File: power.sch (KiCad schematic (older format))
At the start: 21 parts, among them Q1 Q_NMOS_DGS, U7 TPS63060, U8 TPS22929D

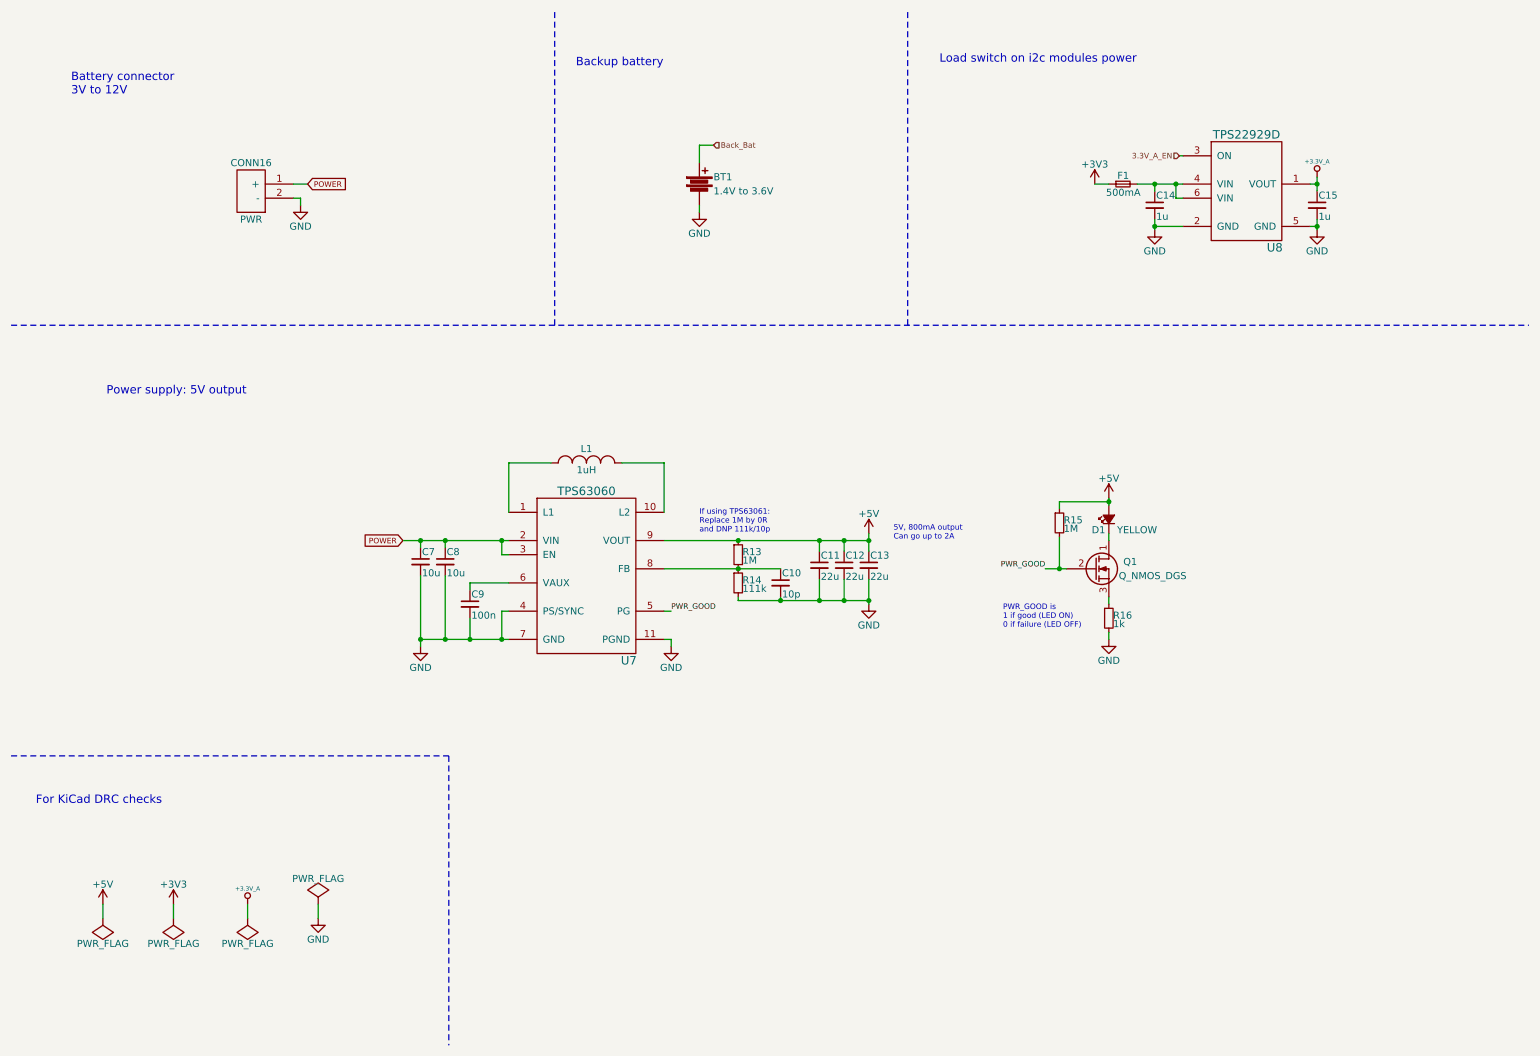
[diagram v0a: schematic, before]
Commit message: Schematics: Minor cleanups & ADC split between 3.3V & 5V
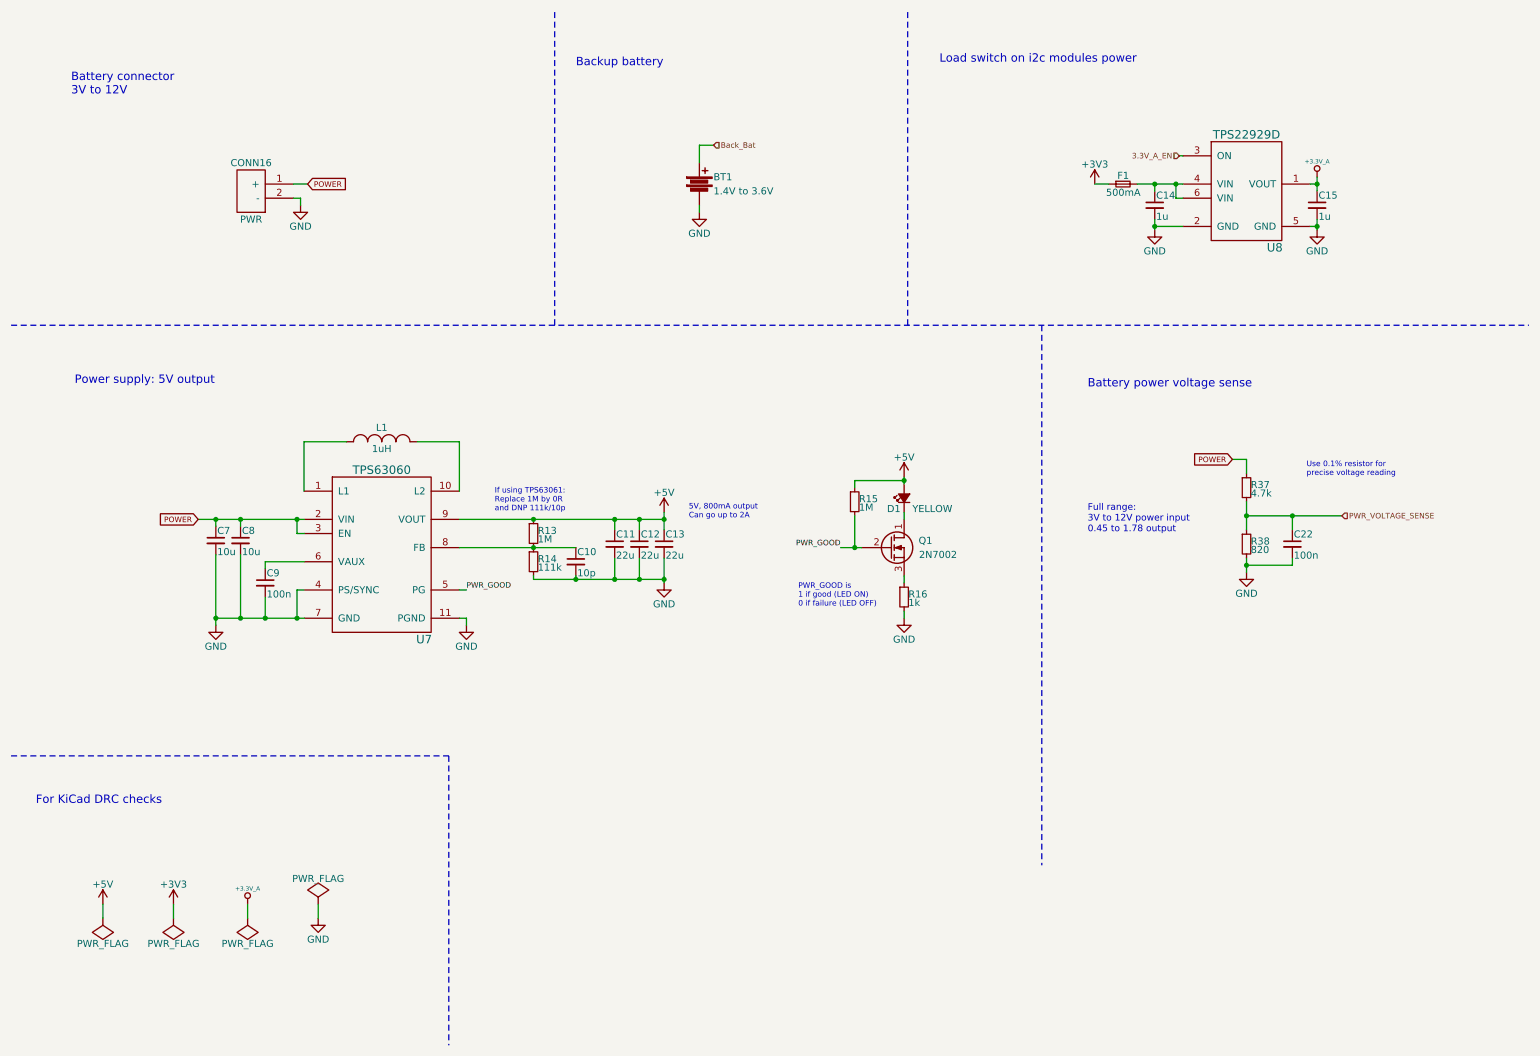
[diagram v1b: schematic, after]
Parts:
- added C22: 100n, symbol C_Small
- added R37: 4.7k, symbol R_Small
- added R38: 820, symbol R_Small
- C10, C11, C12, C13, C14, C15, C7, C8, C9, R13, R14, R15, R16: footprint (none) -> _std:_0402
- CONN16: footprint MODULE -> _connectors:_Pin2mm_2
- Q1: value Q_NMOS_DGS -> 2N7002
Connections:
- net GND: now also C22.2, R38.2
- net POWER: now also R37.1
- new net PWR_VOLTAGE_SENSE: C22.1, R37.2, R38.1
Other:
- note added: "Battery power voltage sense"
- note added: "Full range:\n3V to 12V power input\n0.45 to 1.78 output\n\n"
- note added: "Use 0.1% resistor for \nprecise voltage reading"
- moved on the sheet: C10, C11, C12, C13, C7, C8, C9, D1, L1, Q1, R13, R14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

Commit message: Schematics: Power input overvoltage protection
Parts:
- added D6: ZENER 12V, symbol ZENER
- added F2: 10A, symbol FUSE
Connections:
- net GND: now also D6.2 (A)
- net POWER: now also D6.1 (K), F2.2; no longer CONN16.1 (+)
- new net: CONN16.1 (+), F2.1
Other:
- note added: "Backup battery for RTC"
- note added: "Choose the fuse depending on the type of battery \nyou're using (check the maximum current it can \noutput) so the fuse blows before the battery."
- note added: "Zener diode acts as overvoltage \nprotection. \nWhen input voltage exceeds 12V,\nthe zener diode short circuits the \nbattery to the ground and the fuse \nshould blow."
- note removed: "Backup battery"
- moved on the sheet: CONN16
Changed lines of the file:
@@
 L PWR CONN16
 U 1 1 55AAEB82
-P 2125 1750
-F 0 "CONN16" H 2075 1950 50  0000 C CNN
-F 1 "PWR" H 2075 1550 50  0000 C CNN
-F 2 "_connectors:_Pin2mm_2" H 2375 1750 50  0001 C CNN
-F 3 "DOCUMENTATION" H 2375 1750 50  0001 C CNN
-	1    2125 1750
+P 1500 1650
+F 0 "CONN16" H 1450 1850 50  0000 C CNN
+F 1 "PWR" H 1450 1450 50  0000 C CNN
+F 2 "_connectors:_Pin2mm_2" H 1750 1650 50  0001 C CNN
+F 3 "DOCUMENTATION" H 1750 1650 50  0001 C CNN
+	1    1500 1650
 	-1   0    0    -1
 $EndComp
 $Comp
-L GND #PWR061
+L GND #PWR63
 U 1 1 55AAF05B
-P 2525 1850
-F 0 "#PWR061" H 2525 1600 50  0001 C CNN
-F 1 "GND" H 2525 1700 50  0000 C CNN
-F 2 "" H 2525 1850 60  0000 C CNN
-F 3 "" H 2525 1850 60  0000 C CNN
-	1    2525 1850
-	1    0    0    -1
-$EndComp
-Text GLabel 2575 1700 2    39   Input ~ 0
+P 1900 2150
+F 0 "#PWR63" H 1900 1900 50  0001 C CNN
+F 1 "GND" H 1900 2000 50  0000 C CNN
+F 2 "" H 1900 2150 60  0000 C CNN
+F 3 "" H 1900 2150 60  0000 C CNN
+	1    1900 2150
+	1    0    0    -1
+$EndComp
+Text GLabel 2750 1600 2    39   Input ~ 0
 POWER
 Text GLabel 1800 4075 0    39   Input ~ 0
@@
 $EndComp
 $Comp
-L GND #PWR062
+L GND #PWR64
 U 1 1 55AAFDC8
 P 1925 4825
-F 0 "#PWR062" H 1925 4575 50  0001 C CNN
+F 0 "#PWR64" H 1925 4575 50  0001 C CNN
 F 1 "GND" H 1925 4675 50  0000 C CNN
 F 2 "" H 1925 4825 60  0000 C CNN
@@
 $EndComp
 $Comp
-L GND #PWR063
+L GND #PWR67
 U 1 1 55AAFDF8
 P 3700 4825
-F 0 "#PWR063" H 3700 4575 50  0001 C CNN
+F 0 "#PWR67" H 3700 4575 50  0001 C CNN
 F 1 "GND" H 3700 4675 50  0000 C CNN
 F 2 "" H 3700 4825 60  0000 C CNN
@@
 $EndComp
 $Comp
-L GND #PWR064
+L GND #PWR72
 U 1 1 55AAFF48
 P 6800 4775
-F 0 "#PWR064" H 6800 4525 50  0001 C CNN
+F 0 "#PWR72" H 6800 4525 50  0001 C CNN
 F 1 "GND" H 6800 4625 50  0000 C CNN
 F 2 "" H 6800 4775 60  0000 C CNN
@@
 $EndComp
 $Comp
-L +5V #PWR065
+L +5V #PWR68
 U 1 1 55AB054E
 P 5100 4025
-F 0 "#PWR065" H 5100 3875 50  0001 C CNN
+F 0 "#PWR68" H 5100 3875 50  0001 C CNN
 F 1 "+5V" H 5100 4165 50  0000 C CNN
 F 2 "" H 5100 4025 60  0000 C CNN
@@
 $EndComp
 Wire Wire Line
-	2525 1850 2525 1800
-Wire Wire Line
-	2525 1800 2475 1800
-Wire Wire Line
-	2475 1700 2575 1700
+	1900 2150 1900 1700
+Wire Wire Line
+	1900 1700 1850 1700
+Wire Wire Line
+	1850 1600 1950 1600
 Wire Wire Line
 	3650 4075 5100 4075
@@
 Connection ~ 6450 4275
 $Comp
-L +5V #PWR066
+L +5V #PWR71
 U 1 1 55AB18CE
 P 6800 3775
-F 0 "#PWR066" H 6800 3625 50  0001 C CNN
+F 0 "#PWR71" H 6800 3625 50  0001 C CNN
 F 1 "+5V" H 6800 3915 50  0000 C CNN
 F 2 "" H 6800 3775 60  0000 C CNN
@@
 Connection ~ 4750 4075
 $Comp
-L GND #PWR067
+L GND #PWR69
 U 1 1 55AB26D6
 P 5100 4525
-F 0 "#PWR067" H 5100 4275 50  0001 C CNN
+F 0 "#PWR69" H 5100 4275 50  0001 C CNN
 F 1 "GND" H 5100 4375 50  0000 C CNN
 F 2 "" H 5100 4525 60  0000 C CNN
@@
 $EndComp
 $Comp
-L +3V3 #PWR068
+L +3V3 #PWR73
 U 1 1 55AC1039
 P 8150 1700
-F 0 "#PWR068" H 8150 1550 50  0001 C CNN
+F 0 "#PWR73" H 8150 1550 50  0001 C CNN
 F 1 "+3V3" H 8150 1840 50  0000 C CNN
 F 2 "" H 8150 1700 60  0000 C CNN
@@
 Connection ~ 8575 1700
 $Comp
-L GND #PWR069
+L GND #PWR74
 U 1 1 55AC12A8
 P 8575 2025
-F 0 "#PWR069" H 8575 1775 50  0001 C CNN
+F 0 "#PWR74" H 8575 1775 50  0001 C CNN
 F 1 "GND" H 8575 1875 50  0000 C CNN
 F 2 "" H 8575 2025 60  0000 C CNN
@@
 Connection ~ 8575 2000
 $Comp
-L GND #PWR070
+L GND #PWR77
 U 1 1 55AC13C7
 P 9725 2025
-F 0 "#PWR070" H 9725 1775 50  0001 C CNN
+F 0 "#PWR77" H 9725 1775 50  0001 C CNN
 F 1 "GND" H 9725 1875 50  0000 C CNN
 F 2 "" H 9725 2025 60  0000 C CNN
@@
 Connection ~ 9725 2000
 $Comp
-L +3.3V_A #PWR071
+L +3.3V_A #PWR76
 U 1 1 55AC15A6
 P 9725 1650
-F 0 "#PWR071" H 9725 1610 30  0001 C CNN
+F 0 "#PWR76" H 9725 1610 30  0001 C CNN
 F 1 "+3.3V_A" H 9725 1760 30  0000 C CNN
 F 2 "" H 9725 1650 60  0000 C CNN
@@
 $EndComp
 $Comp
-L GND #PWR072
+L GND #PWR70
 U 1 1 55ACA99A
 P 5350 1900
-F 0 "#PWR072" H 5350 1650 50  0001 C CNN
+F 0 "#PWR70" H 5350 1650 50  0001 C CNN
 F 1 "GND" H 5350 1750 50  0000 C CNN
 F 2 "" H 5350 1900 60  0000 C CNN
@@
 	5450 1425 5350 1425
 Text Notes 4475 875  0    59   ~ 0
-Backup battery
-Text Notes 925  3125 0    59   ~ 0
+Backup battery for RTC
+Text Notes 800  3075 0    59   ~ 0
 Power supply: 5V output
-Text Notes 900  1075 0    59   ~ 0
+Text Notes 775  975  0    59   ~ 0
 Battery connector\n3V to 12V
 Text Notes 7050 850  0    59   ~ 0
@@
 	4325 2700 4325 475
 $Comp
-L PWR_FLAG #FLG073
+L PWR_FLAG #FLG2
 U 1 1 55B1438E
 P 1625 6900
-F 0 "#FLG073" H 1625 6995 50  0001 C CNN
+F 0 "#FLG2" H 1625 6995 50  0001 C CNN
 F 1 "PWR_FLAG" H 1625 7080 50  0000 C CNN
 F 2 "" H 1625 6900 60  0000 C CNN
@@
 $EndComp
 $Comp
-L +3V3 #PWR074
+L +3V3 #PWR62
 U 1 1 55B143F6
 P 1625 6800
-F 0 "#PWR074" H 1625 6650 50  0001 C CNN
+F 0 "#PWR62" H 1625 6650 50  0001 C CNN
 F 1 "+3V3" H 1625 6940 50  0000 C CNN
 F 2 "" H 1625 6800 60  0000 C CNN
@@
 	1625 6800 1625 6900
 $Comp
-L +3.3V_A #PWR075
+L +3.3V_A #PWR65
 U 1 1 55B144F4
 P 2150 6800
-F 0 "#PWR075" H 2150 6760 30  0001 C CNN
+F 0 "#PWR65" H 2150 6760 30  0001 C CNN
 F 1 "+3.3V_A" H 2150 6910 30  0000 C CNN
 F 2 "" H 2150 6800 60  0000 C CNN
@@
 $EndComp
 $Comp
-L PWR_FLAG #FLG076
+L PWR_FLAG #FLG3
 U 1 1 55B1455A
 P 2150 6900
-F 0 "#FLG076" H 2150 6995 50  0001 C CNN
+F 0 "#FLG3" H 2150 6995 50  0001 C CNN
 F 1 "PWR_FLAG" H 2150 7080 50  0000 C CNN
 F 2 "" H 2150 6900 60  0000 C CNN
@@
 $EndComp
 $Comp
-L PWR_FLAG #FLG077
+L PWR_FLAG #FLG1
 U 1 1 55B145A4
 P 1125 6900
-F 0 "#FLG077" H 1125 6995 50  0001 C CNN
+F 0 "#FLG1" H 1125 6995 50  0001 C CNN
 F 1 "PWR_FLAG" H 1125 7080 50  0000 C CNN
 F 2 "" H 1125 6900 60  0000 C CNN
@@
 $EndComp
 $Comp
-L +5V #PWR078
+L +5V #PWR61
 U 1 1 55B145DB
 P 1125 6800
-F 0 "#PWR078" H 1125 6650 50  0001 C CNN
+F 0 "#PWR61" H 1125 6650 50  0001 C CNN
 F 1 "+5V" H 1125 6940 50  0000 C CNN
 F 2 "" H 1125 6800 60  0000 C CNN
@@
 	2150 6800 2150 6900
 $Comp
-L PWR_FLAG #FLG079
+L PWR_FLAG #FLG4
 U 1 1 55B14718
 P 2650 6800
-F 0 "#FLG079" H 2650 6895 50  0001 C CNN
+F 0 "#FLG4" H 2650 6895 50  0001 C CNN
 F 1 "PWR_FLAG" H 2650 6980 50  0000 C CNN
 F 2 "" H 2650 6800 60  0000 C CNN
@@
 $EndComp
 $Comp
-L GND #PWR080
+L GND #PWR66
 U 1 1 55B1474F
 P 2650 6900
-F 0 "#PWR080" H 2650 6650 50  0001 C CNN
+F 0 "#PWR66" H 2650 6650 50  0001 C CNN
 F 1 "GND" H 2650 6750 50  0000 C CNN
 F 2 "" H 2650 6900 60  0000 C CNN
@@
 $EndComp
 $Comp
-L GND #PWR081
+L GND #PWR75
 U 1 1 55B3D2C4
 P 9225 4450
-F 0 "#PWR081" H 9225 4200 50  0001 C CNN
+F 0 "#PWR75" H 9225 4200 50  0001 C CNN
 F 1 "GND" H 9225 4300 50  0000 C CNN
 F 2 "" H 9225 4450 60  0000 C CNN
@@
 $EndComp
 Wire Wire Line
-	9900 4050 9225 4050
+	9225 4050 9900 4050
 Wire Wire Line
 	9225 3950 9225 4150
@@
 Connection ~ 9550 4050
 Wire Wire Line
-	9225 4450 9225 4350
+	9225 4350 9225 4450
 Wire Wire Line
 	9550 4350 9550 4400
@@
 Text Notes 8100 4250 0    47   ~ 0
 Full range:\n3V to 12V power input\n0.45 to 1.78 output\n\n
+$Comp
+L FUSE F2
+U 1 1 55B4BB3E
+P 2200 1600
+F 0 "F2" H 2300 1650 50  0000 C CNN
+F 1 "10A" H 2100 1550 50  0000 C CNN
+F 2 "" H 2200 1600 60  0000 C CNN
+F 3 "" H 2200 1600 60  0000 C CNN
+	1    2200 1600
+	1    0    0    -1
+$EndComp
+$Comp
+L ZENER D6
+U 1 1 55B4BCD5
+P 2600 1850
+F 0 "D6" H 2600 1950 50  0000 C CNN
+F 1 "ZENER 12V" H 2600 1750 50  0000 C CNN
+F 2 "" H 2600 1850 60  0000 C CNN
+F 3 "" H 2600 1850 60  0000 C CNN
+	1    2600 1850
+	0    1    1    0
+$EndComp
+Wire Wire Line
+	2450 1600 2750 1600
+Wire Wire Line
+	2600 1600 2600 1650
+Wire Wire Line
+	2600 2050 2600 2100
+Wire Wire Line
+	2600 2100 1900 2100
+Connection ~ 1900 2100
+Connection ~ 2600 1600
+Text Notes 2875 2100 0    39   ~ 0
+Zener diode acts as overvoltage \nprotection. \nWhen input voltage exceeds 12V,\nthe zener diode short circuits the \nbattery to the ground  and the fuse \nshould blow.
+Text Notes 1750 1350 0    39   ~ 0
+Choose the fuse depending on the type of battery \nyou're using (check the maximum current it can \noutput) so the fuse blows before the battery.
 $EndSCHEMATC

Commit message: Netlist
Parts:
- BT1: footprint (none) -> _connectors:BK-885
- C10, C11, C12, C13, C14, C15, C7, C8, C9: footprint _std:_0402 -> Capacitors_SMD:C_0402
- C22: footprint (none) -> Capacitors_SMD:C_0402
- D1: footprint (none) -> LEDs:LED-0603
- D6: footprint (none) -> Diodes_SMD:Diode-SMA_Standard
- F1: footprint (none) -> Resistors_SMD:R_0805
- F2: footprint (none) -> Resistors_SMD:R_1206
- L1: footprint (none) -> inductors:Laird_TYS6045
- Q1: footprint (none) -> _std:_SOT23-3
- R13, R14, R15, R16: footprint _std:_0402 -> Resistors_SMD:R_0402
- R37, R38: footprint (none) -> Resistors_SMD:R_0402
- U7: footprint (none) -> _std:WSON10
- U8: footprint (none) -> _std:_TSOT23-6
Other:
- note added: "Zener diode acts as overvoltage \nprotection. \nWhen input voltage exceeds 12V,\nthe zener diode short circuits the \nbattery to the ground and the fuse \nshould blow.\n\nIf you don't want this, don't place the diode."
- note removed: "Zener diode acts as overvoltage \nprotection. \nWhen input voltage exceeds 12V,\nthe zener diode short circuits the \nbattery to the ground and the fuse \nshould blow."
